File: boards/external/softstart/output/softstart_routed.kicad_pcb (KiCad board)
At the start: 4 copper layers, 150 x 100 mm, 78 parts, among them J1 TB, J2 TB, J3 TB, J4 TB, J5 SWD, Q1A IRFB4110, Q1B IRFB4110, Q2A IRFB4110, Q2B IRFB4110, Q5 AO3400, Q6 AO3400, Q7 2N7002, Q8 2N7002, SW1 RESET, U1 STM32G031K8T6, U2 H11AA1, U3 INA180A3, U4 XC6206-3.3V, U5 UCC27211, U6 UCC27211, U7 LM393, U8 MCP6001, U9 LM7812

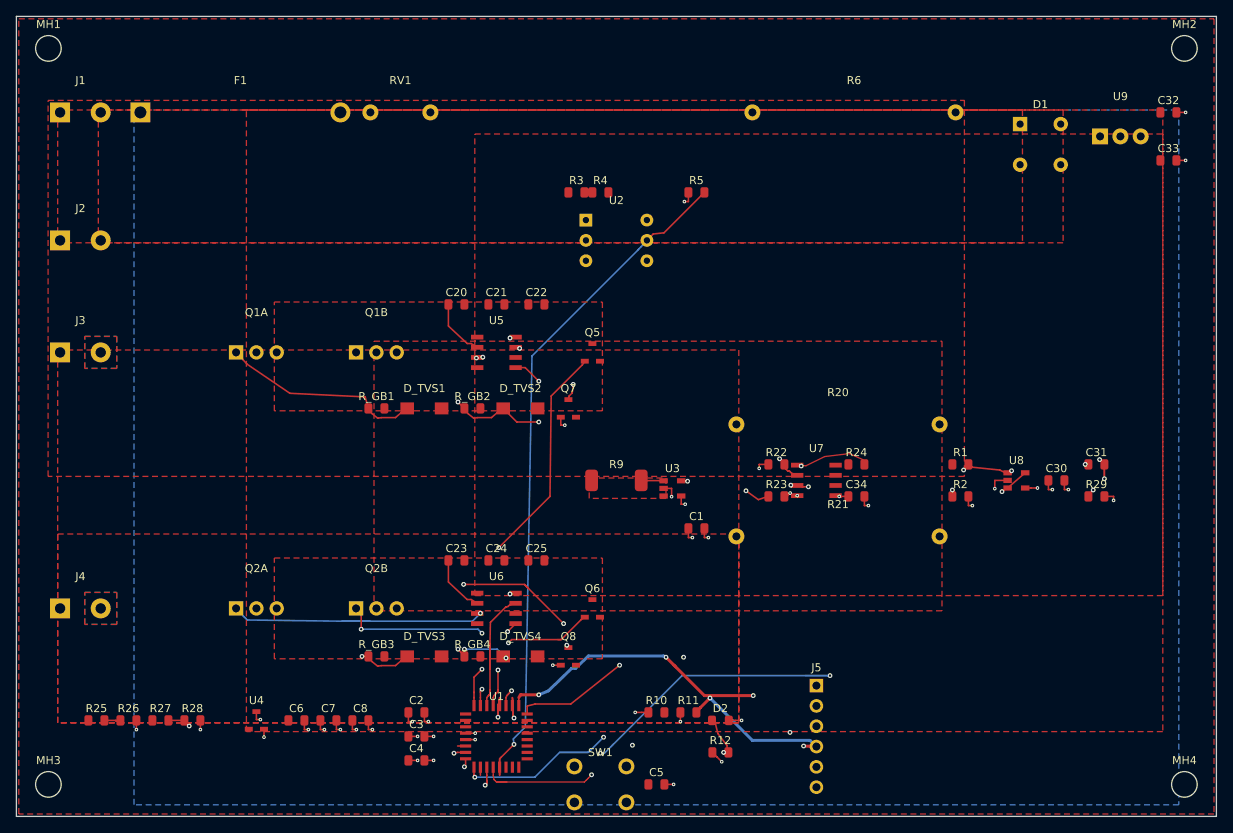
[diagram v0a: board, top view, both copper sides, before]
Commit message: fix(softstart): close all pour/routed-net opens + harden the copper gate (PR #3481 review, refs #3343)
Judge blocker: AC_NEUTRAL and ISENSE_POS pours had fill enabled but zero
filled polygons (shadowed/carved by sibling zones) -- both nets were
electrically open in the committed artifact, masked by the analyzer's
boundary-polygon false positive (issue #3482).

Recipe rework (single-rectangle-per-net pours cannot tile this board):
- Pour only what is geometrically sound: GND -> In1.Cu plane, +3.3V ->
  In2.Cu plane, SCAP_*_GND single-pad ties.  The other 11 power nets
  are ROUTED as 0.3-0.4 mm skeletons via a --net-class-map sidecar and
  bulked with F.Cu reinforcement pours; zero-fill reinforcement zones
  are deleted (the skeleton carries the net).
- ROUTE_FIRST_NETS (BUS_LINE / VRECT / V_BANK_POS_SENSE / UCC_LO_NEG)
  carry net-class priority 1 so they commit before congestion builds;
  measured at uniform ordering they end partial/blocked_path.
- Recovery pass (--preserve-existing, #3155) re-routes main-pass
  stragglers against a frozen board (closes I_SENSE_OUT).
- Step-10b B.Cu bridge pour + via-in-pad anchors for islanded supply
  nets (closes VGATE's U6-cluster island).
- Step-10c drill-to-drill repair (NRST via inside SW1.2's TH drill).
- Step-10d cross-net segment/via clearance repair (a SRC_NEG via
  physically overlapped a UCC_LO_NEG trace -- a short invisible to the
  same-net connectivity audit; 4 conflicts repaired).
- Hardened step-12 gate: every power/bridged net must be geometrically
  continuous (shapely copper union, all pads in ONE component) and no
  fill-enabled zone may have zero filled polygons; shapely missing =>
  gate FAILS.  Does not wait for the #3482 analyzer fix.

Router fix: snap synthetic Steiner branch points onto the routing grid
(build_rsmt snap_fn).  Off-grid virtual pads have no sub-grid rescue
and fail pin_access with PADS_OFF_GRID -- the multi-terminal power-net
signature that blocked the skeleton-routing strategy.

Measured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
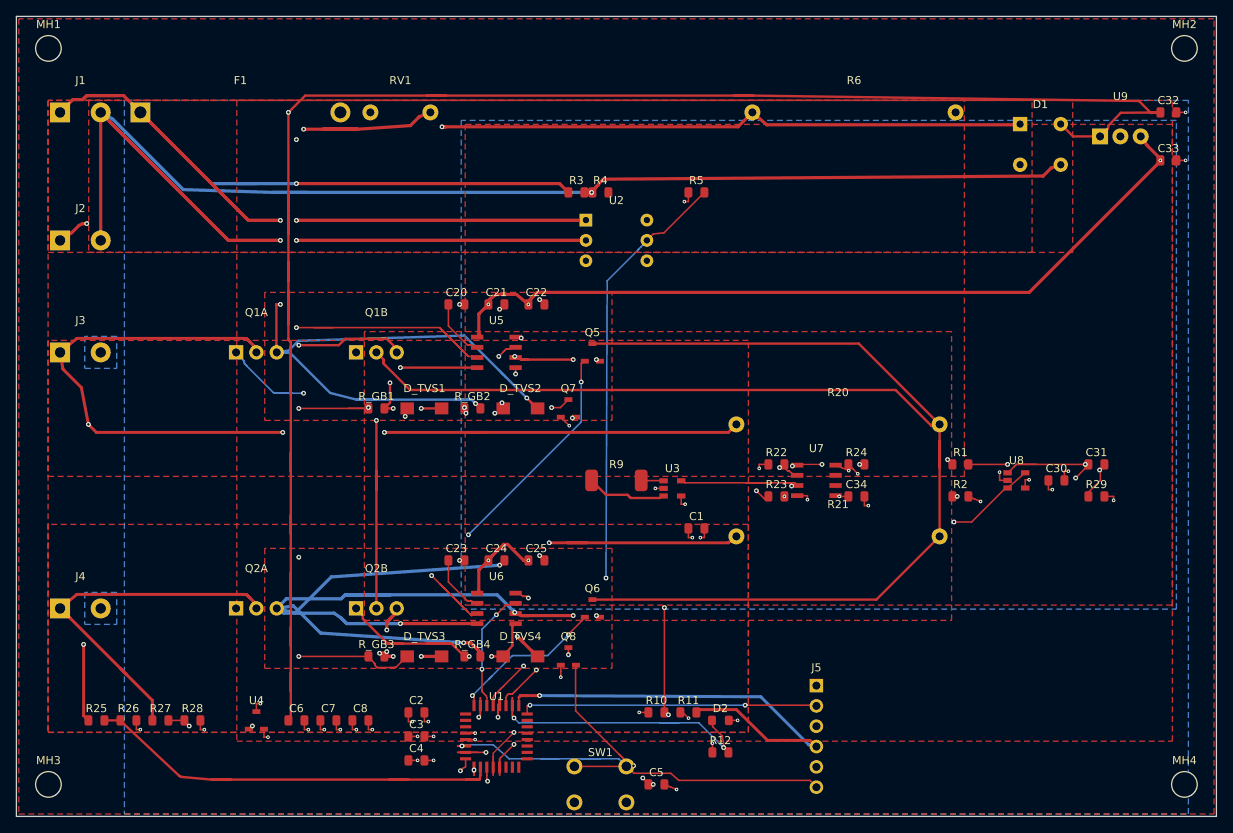
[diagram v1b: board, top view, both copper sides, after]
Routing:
- net VRECT: track 0.00 -> 280.6 mm, vias 0 -> 2
- net SRC_POS: track 0.00 -> 256.6 mm, vias 0 -> 14
- net SRC_NEG: track 0.00 -> 253.7 mm, vias 0 -> 14
- net AC_NEUTRAL: track 0.00 -> 251.1 mm, vias 0 -> 4
- net BUS_LINE: track 0.00 -> 214.8 mm, vias 0 -> 1
- net AC_LINE: track 0.00 -> 189.5 mm, vias 0 -> 4
- net FUSED_LINE: track 0.00 -> 169.6 mm, vias 0 -> 3
- net NRST: track 1.00 -> 159.1 mm, vias 0 -> 7
- net SCAP_POS+: track 0.00 -> 155.5 mm, vias 0 -> 4
- net SCAP_NEG+: track 0.00 -> 132.6 mm, vias 0 -> 1
- net VGATE: track 0.00 -> 113.3 mm, vias 0 -> 5
- net V_BANK_POS_SENSE: track 3.65 -> 51.3 mm
- net UCC_HO_POS: track 75.5 -> 105.3 mm, vias 3 -> 6
- net V_AC_SENSE_RAW: track 20.5 -> 44.2 mm
- net UCC_LO_NEG: track 45.8 -> 25.8 mm, vias 6 -> 2
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- added copper zone on B.Cu, net VGATE
- removed copper zone on F.Cu, net ISENSE_POS
- removed copper zone on F.Cu, net SCAP_NEG_GND
- removed copper zone on F.Cu, net SCAP_POS_GND

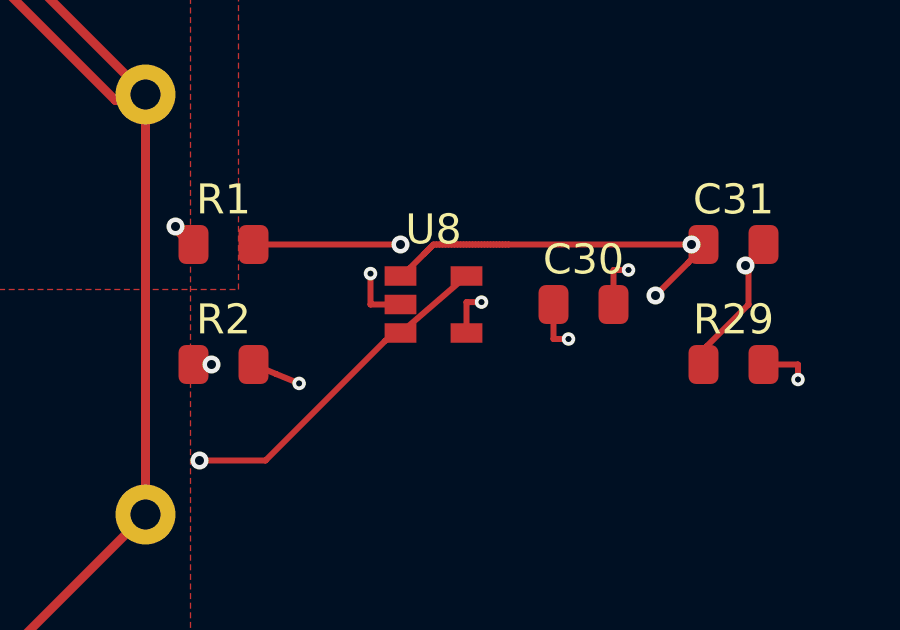
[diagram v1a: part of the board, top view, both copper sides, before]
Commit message: fix(softstart): clear final intra-IC clearance violation — 0 DRC (closes #3480) (#3493)
* fix(router): validate intra-IC routes against pad clearance + perimeter-wrap fallback (refs #3480)

create_intra_ic_routes previously emitted direct pin-to-pin segments
blindly; on softstart's U8 (SOT-23-5) the pin1->pin4 V_AC_SENSE diagonal
passed 0.027mm from the GND pad where 0.102mm is required. Emitted
segments are now validated edge-to-edge against same-package foreign
pads at the active clearance; on violation a package-perimeter wrap is
tried (validated against nearby foreign pads and previously routed
copper), and if no legal wrap exists the pair is deferred to the main
A* router instead of being marked connected.

Co-Authored-By: Claude Opus 4.7 <noreply@anthropic.com>

* fix(softstart): reroute U8 intra-IC V_AC_SENSE tie around package — 0 DRC at jlcpcb-tier1 (closes #3480)

Replace the single violating pin1->pin4 diagonal (0.027mm from the U8
GND pad) with a 4-segment perimeter wrap over pin 5 and down the east
side of the package (>=0.27mm clearance to every foreign pad, trace,
and via). All other committed geometry is untouched.

Measured on the committed artifact:
- kct check --mfr jlcpcb-tier1: 0 errors (was 1)
- NetStatusAnalyzer: 41/41 nets complete (37 routed + 4 pour)
- _audit_pour_nets geometric copper-union audit: all power nets +
  V_AC_SENSE/STATUS_LED/VGATE continuous, no zero-fill zones
- Manufacturing bundle re-exported (gerbers, BOM/CPL, report, manifest)

Co-Authored-By: Claude Opus 4.7 <noreply@anthropic.com>

---------

Co-authored-by: Claude Opus 4.7 <noreply@anthropic.com>
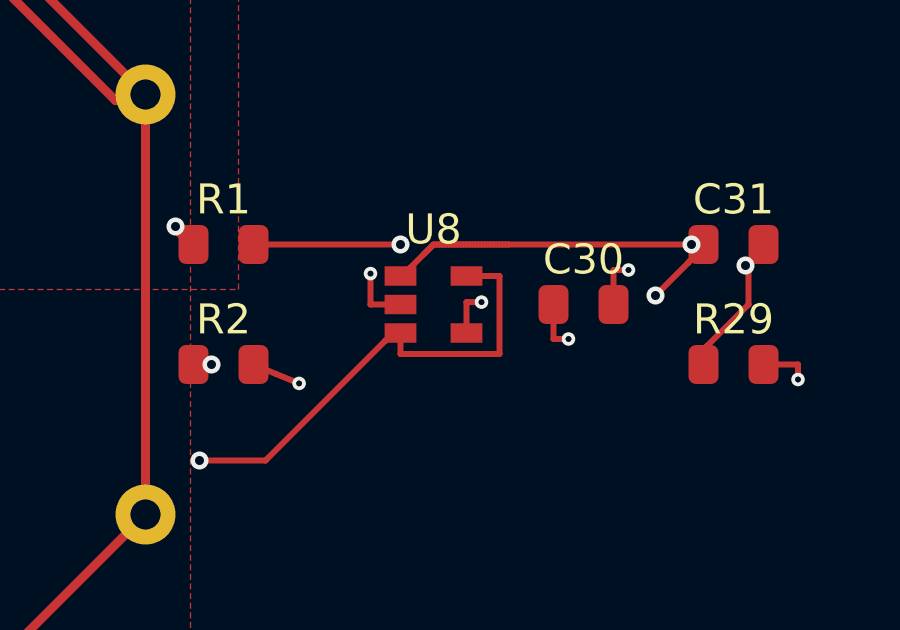
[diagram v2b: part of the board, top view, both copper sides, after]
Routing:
- net V_AC_SENSE: track 86.3 -> 91.1 mm
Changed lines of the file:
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@@
 		(net 15)
 	)
-	(segment
-		(start 223.9 158.95)
-		(end 226.1 157.05)
-		(width 0.2)
-		(layer "F.Cu")
-		(net 15)
-	)
 	(via
 		(at 217.2 163.2)
@@
 	)
 	(embedded_fonts no)
+	(segment
+		(start 223.9 158.95)
+		(end 223.9 159.65)
+		(width 0.2)
+		(layer "F.Cu")
+		(net 15)
+	)
+	(segment
+		(start 223.9 159.65)
+		(end 227.2 159.65)
+		(width 0.2)
+		(layer "F.Cu")
+		(net 15)
+	)
+	(segment
+		(start 227.2 159.65)
+		(end 227.2 157.05)
+		(width 0.2)
+		(layer "F.Cu")
+		(net 15)
+	)
+	(segment
+		(start 227.2 157.05)
+		(end 226.1 157.05)
+		(width 0.2)
+		(layer "F.Cu")
+		(net 15)
+	)
 )

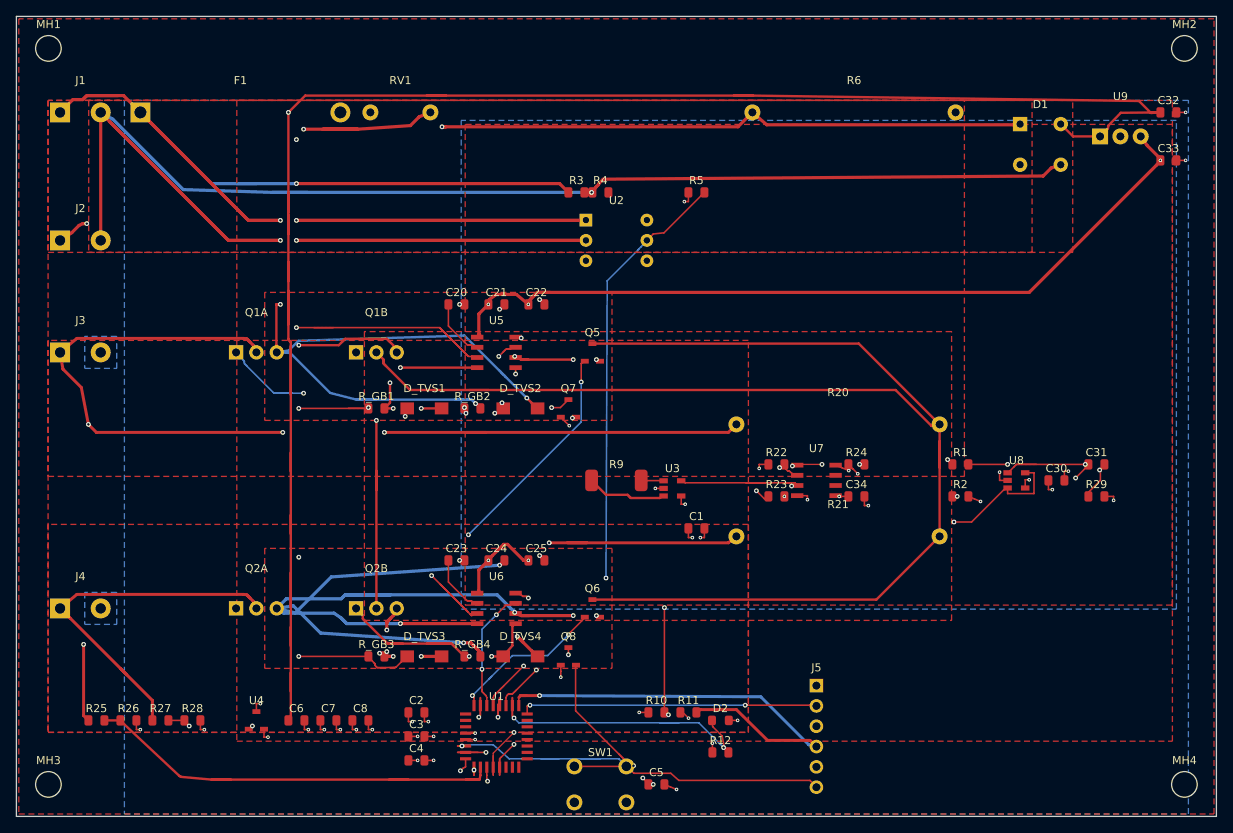
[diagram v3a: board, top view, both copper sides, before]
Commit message: fix(router): 45° quantization in post-route mutation passes (closes #3532)
204/4519 segments on softstart's committed routed artifact sat 0.8-22.5°
off the 0/45/90/135 set; every fleet board carried the same class
(board 07: 297/909). Attribution: 127 pad-tail emissions (the C++
reconstruct_path / Python _convert_path_to_route connect the last grid
cell to the exact off-grid pad centre with one skewed segment), 41
step-10c/d repair chain drags (regex endpoint dragging in
generate_design.py), 36 optimizer mutations (pull-tight neighbour
re-aiming, chamfer terminal restoration).

Fixes at source, all sharing the new router/quantize.py helpers
(is_45_aligned / snap_direction_8 / dogleg_points / quantize_pcb_file):

* cpp_backend._convert_result_to_route splits skewed C++ tails into
  exact float64 doglegs (C++ float32 ulp is too coarse for exact legs)
* Python Router._convert_path_to_route emits dogleg pad tails; the
  extend-to-pad branch requires the extended segment to stay aligned
* convert_corners_45 terminal restoration emits doglegs, not skews
* pull_tight_pass declines windows whose neighbours are not parallel
  to the translation direction (the classic H-V-H jog still compresses)
* drc_nudge segment/via chain snaps decline drags that would skew an
  abutting segment off the 45° set
* softstart recipe: step-10c via slides snap to the 8-direction set;
  new step-10e runs quantize_pcb_file before the DRC gate

Committed artifacts repaired in place with the exact-decimal
quantize_pcb_file (dogleg endpoints preserved bit-for-bit, second-leg
uuids deterministic uuid5). Fleet census ratchet in
tests/test_fleet_45_census.py: softstart + boards 01-05 at 0 off-angle;
documented residuals (issue #3535) are 2 corridor chords where both
dogleg variants collide (06/07) and board 07's 55 DDR_DATA_BYTE_0
length-tuning meanders (doglegging breaks the exactly-tuned
match_group_length_skew).

DRC: softstart 0 violations at jlcpcb-tier1 (strict gate; manufacturers
override added 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
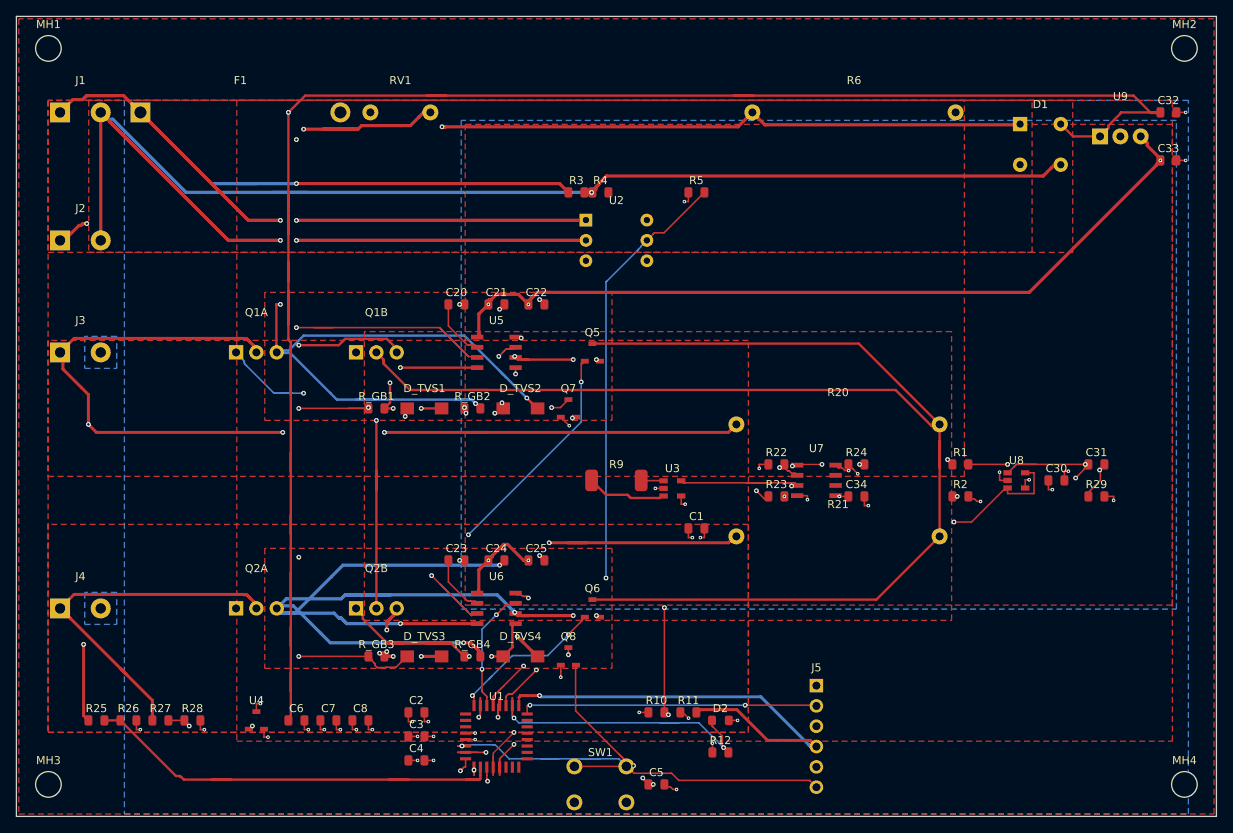
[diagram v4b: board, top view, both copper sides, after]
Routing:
- net SRC_NEG: track 253.7 -> 257.0 mm
- net V_BUS_DVDT: track 102.5 -> 105.6 mm
- net SRC_POS: track 256.6 -> 257.8 mm
- net AC_NEUTRAL: track 251.1 -> 252.0 mm
- net FUSED_LINE: track 169.6 -> 170.5 mm
- net SCAP_NEG+: track 132.6 -> 133.4 mm
- net SCAP_POS+: track 155.5 -> 156.1 mm
- net NRST: track 159.1 -> 159.6 mm
